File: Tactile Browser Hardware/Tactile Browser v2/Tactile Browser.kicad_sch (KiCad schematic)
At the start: 135 parts, among them SW1 SW_Push, SW10 SW_Push, SW11 SW_Push, SW12 SW_Push, SW13 SW_Push, SW14 SW_Push, SW15 SW_Push, SW16 SW_Push, SW17 SW_Push, SW18 SW_Push, SW2 SW_Push, SW3 SW_Push, SW4 SW_Push, SW5 SW_Push, SW6 SW_Push, SW7 SW_Push, SW8 SW_Push, SW9 SW_Push

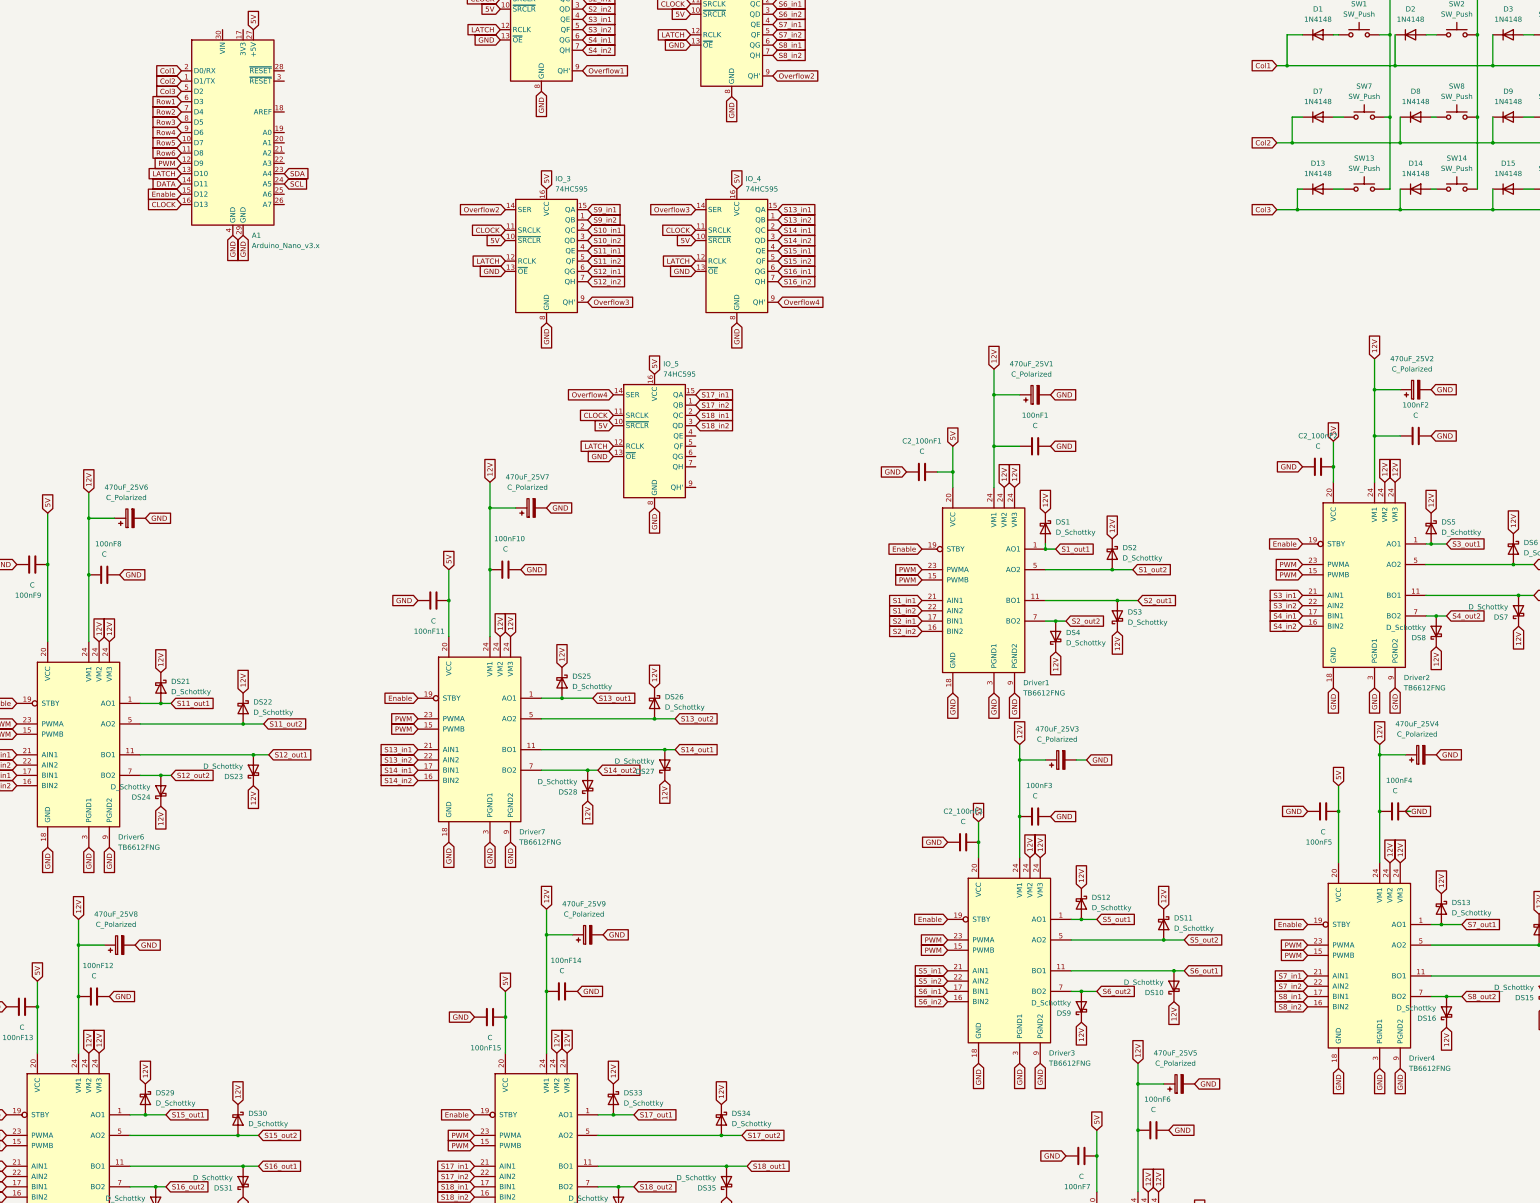
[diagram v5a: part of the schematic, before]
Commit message: updated capacitors
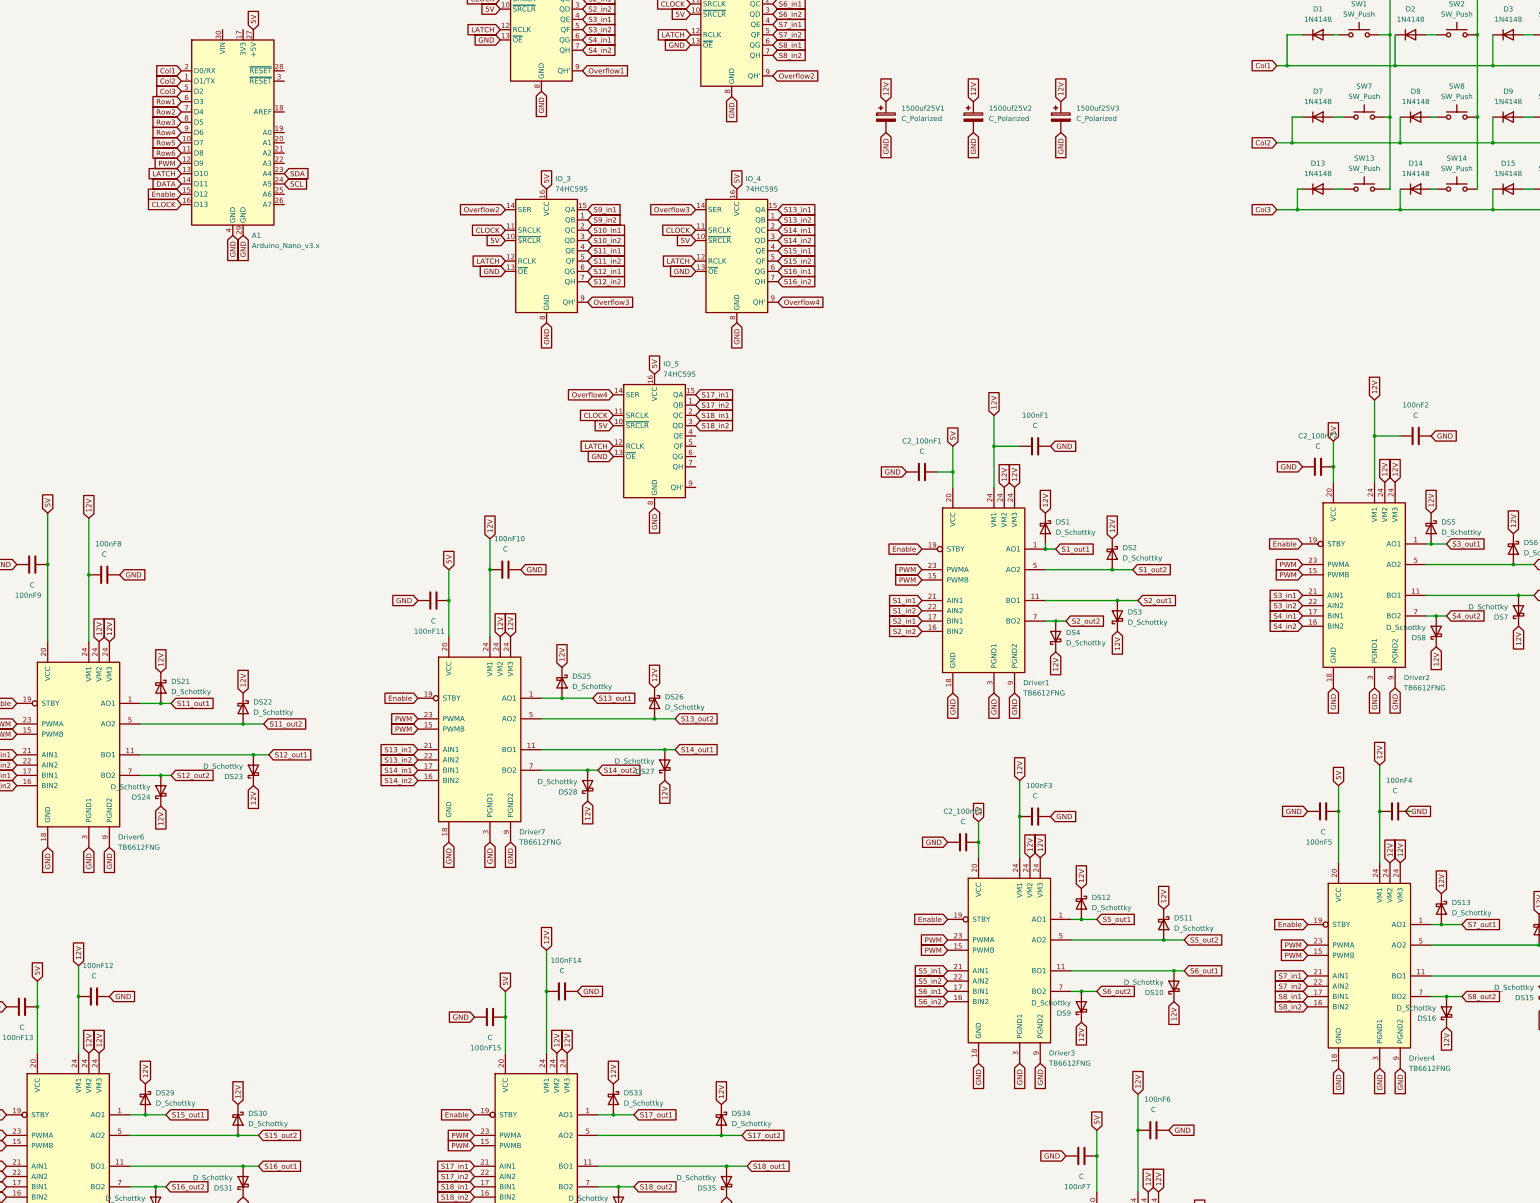
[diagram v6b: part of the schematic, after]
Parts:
- removed 470uF_25V1, 470uF_25V2, 470uF_25V3, 470uF_25V4, 470uF_25V5, 470uF_25V6, 470uF_25V7, 470uF_25V8, 470uF_25V9: C_Polarized, Capacitor_SMD:CP_Elec_8x10, symbol Device:C_Polarized
- added 1500uf25V1, 1500uf25V2, 1500uf25V3: C_Polarized, Capacitor_SMD:CP_Elec_8x10, symbol Device:C_Polarized
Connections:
- net 12V: now also 1500uf25V1.1, 1500uf25V2.1, 1500uf25V3.1
- net GND: now also 1500uf25V1.2, 1500uf25V2.2, 1500uf25V3.2

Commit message: changed to vertical screw terminals
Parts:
- removed 1500uf25V2, 1500uf25V3: C_Polarized, Capacitor_SMD:CP_Elec_8x10, symbol Device:C_Polarized
- added 1000uf25V2, 1000uf25V3, 1000uf25V4: C_Polarized, Capacitor_SMD:CP_Elec_10x12.5, symbol Device:C_Polarized
- 100uf25V1: renamed from 1500uf25V1; footprint Capacitor_SMD:CP_Elec_8x10 -> Capacitor_SMD:CP_Elec_10x12.5
- Sol1: renamed from Solenoid1; footprint TerminalBlock_Phoenix:TerminalBlock_Phoenix_MKDS-1,5-2-5.08_1x02_P5.08mm_Horizontal -> TerminalBlock_Phoenix:ScrewTerminal_Vertical_1935310
- Sol10: renamed from Solenoid10; footprint TerminalBlock_Phoenix:TerminalBlock_Phoenix_MKDS-1,5-2-5.08_1x02_P5.08mm_Horizontal -> TerminalBlock_Phoenix:ScrewTerminal_Vertical_1935310
- Sol11: renamed from Solenoid11; footprint TerminalBlock_Phoenix:TerminalBlock_Phoenix_MKDS-1,5-2-5.08_1x02_P5.08mm_Horizontal -> TerminalBlock_Phoenix:ScrewTerminal_Vertical_1935310
- Sol12: renamed from Solenoid12; footprint TerminalBlock_Phoenix:TerminalBlock_Phoenix_MKDS-1,5-2-5.08_1x02_P5.08mm_Horizontal -> TerminalBlock_Phoenix:ScrewTerminal_Vertical_1935310
- Sol13: renamed from Solenoid13; footprint TerminalBlock_Phoenix:TerminalBlock_Phoenix_MKDS-1,5-2-5.08_1x02_P5.08mm_Horizontal -> TerminalBlock_Phoenix:ScrewTerminal_Vertical_1935310
- Sol14: renamed from Solenoid14; footprint TerminalBlock_Phoenix:TerminalBlock_Phoenix_MKDS-1,5-2-5.08_1x02_P5.08mm_Horizontal -> TerminalBlock_Phoenix:ScrewTerminal_Vertical_1935310
- Sol15: renamed from Solenoid15; footprint TerminalBlock_Phoenix:TerminalBlock_Phoenix_MKDS-1,5-2-5.08_1x02_P5.08mm_Horizontal -> TerminalBlock_Phoenix:ScrewTerminal_Vertical_1935310
- Sol16: renamed from Solenoid16; footprint TerminalBlock_Phoenix:TerminalBlock_Phoenix_MKDS-1,5-2-5.08_1x02_P5.08mm_Horizontal -> TerminalBlock_Phoenix:ScrewTerminal_Vertical_1935310
- Sol17: renamed from Solenoid17; footprint TerminalBlock_Phoenix:TerminalBlock_Phoenix_MKDS-1,5-2-5.08_1x02_P5.08mm_Horizontal -> TerminalBlock_Phoenix:ScrewTerminal_Vertical_1935310
- Sol18: renamed from Solenoid18; footprint TerminalBlock_Phoenix:TerminalBlock_Phoenix_MKDS-1,5-2-5.08_1x02_P5.08mm_Horizontal -> TerminalBlock_Phoenix:ScrewTerminal_Vertical_1935310
- Sol2: renamed from Solenoid2; footprint TerminalBlock_Phoenix:TerminalBlock_Phoenix_MKDS-1,5-2-5.08_1x02_P5.08mm_Horizontal -> TerminalBlock_Phoenix:ScrewTerminal_Vertical_1935310
- Sol3: renamed from Solenoid3; footprint TerminalBlock_Phoenix:TerminalBlock_Phoenix_MKDS-1,5-2-5.08_1x02_P5.08mm_Horizontal -> TerminalBlock_Phoenix:ScrewTerminal_Vertical_1935310
- Sol4: renamed from Solenoid4; footprint TerminalBlock_Phoenix:TerminalBlock_Phoenix_MKDS-1,5-2-5.08_1x02_P5.08mm_Horizontal -> TerminalBlock_Phoenix:ScrewTerminal_Vertical_1935310
- Sol5: renamed from Solenoid5; footprint TerminalBlock_Phoenix:TerminalBlock_Phoenix_MKDS-1,5-2-5.08_1x02_P5.08mm_Horizontal -> TerminalBlock_Phoenix:ScrewTerminal_Vertical_1935310
- Sol6: renamed from Solenoid6; footprint TerminalBlock_Phoenix:TerminalBlock_Phoenix_MKDS-1,5-2-5.08_1x02_P5.08mm_Horizontal -> TerminalBlock_Phoenix:ScrewTerminal_Vertical_1935310
- Sol7: renamed from Solenoid7; footprint TerminalBlock_Phoenix:TerminalBlock_Phoenix_MKDS-1,5-2-5.08_1x02_P5.08mm_Horizontal -> TerminalBlock_Phoenix:ScrewTerminal_Vertical_1935310
- Sol8: renamed from Solenoid8; footprint TerminalBlock_Phoenix:TerminalBlock_Phoenix_MKDS-1,5-2-5.08_1x02_P5.08mm_Horizontal -> TerminalBlock_Phoenix:ScrewTerminal_Vertical_1935310
- Sol9: renamed from Solenoid9; footprint TerminalBlock_Phoenix:TerminalBlock_Phoenix_MKDS-1,5-2-5.08_1x02_P5.08mm_Horizontal -> TerminalBlock_Phoenix:ScrewTerminal_Vertical_1935310
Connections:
- net 12V: now also 1000uf25V2.1, 1000uf25V3.1, 1000uf25V4.1
- net GND: now also 1000uf25V2.2, 1000uf25V3.2, 1000uf25V4.2
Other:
- moved on the sheet: Sol15, Sol16

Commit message: solenoid wiring!!
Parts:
- 12V_supply1: footprint TerminalBlock_Altech:Altech_AK100_1x02_P5.00mm -> TerminalBlock_Phoenix:ScrewTerminal_Vertical_1935310
- 5V_logic_rail1, I2C_bus1: footprint TerminalBlock:TerminalBlock_Xinya_XY308-2.54-2P_1x02_P2.54mm_Horizontal -> Connector_JST:JST_PH_B2B-PH-SM4-TB_1x02-1MP_P2.00mm_Vertical
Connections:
- net Enable renamed STBY
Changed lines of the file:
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@@
 		)
 	)
-	(global_label "Enable"
+	(global_label "STBY"
 		(shape input)
 		(at 422.91 172.72 180)
@@
 		)
 		(property "Intersheetrefs" "${INTERSHEET_REFS}"
-			(at 413.575 172.72 0)
+			(at 415.3891 172.72 0)
 			(effects
 				(font
@@
 		)
 	)
-	(global_label "Enable"
+	(global_label "STBY"
 		(shape input)
 		(at 218.44 313.69 180)
@@
 		)
 		(property "Intersheetrefs" "${INTERSHEET_REFS}"
-			(at 209.105 313.69 0)
+			(at 210.9191 313.69 0)
 			(effects
 				(font
@@
 		)
 	)
-	(global_label "Enable"
+	(global_label "STBY"
 		(shape input)
 		(at 335.28 265.43 180)
@@
 		)
 		(property "Intersheetrefs" "${INTERSHEET_REFS}"
-			(at 325.945 265.43 0)
+			(at 327.7591 265.43 0)
 			(effects
 				(font
@@
 		)
 	)
-	(global_label "Enable"
+	(global_label "STBY"
 		(shape input)
 		(at 146.05 86.36 180)
@@
 		)
 		(property "Intersheetrefs" "${INTERSHEET_REFS}"
-			(at 136.715 86.36 0)
+			(at 138.5291 86.36 0)
 			(effects
 				(font
@@
 		)
 	)
-	(global_label "Enable"
+	(global_label "STBY"
 		(shape input)
 		(at 204.47 210.82 180)
@@
 		)
 		(property "Intersheetrefs" "${INTERSHEET_REFS}"
-			(at 195.135 210.82 0)
+			(at 196.9491 210.82 0)
 			(effects
 				(font
@@
 		)
 	)
-	(global_label "Enable"
+	(global_label "STBY"
 		(shape input)
 		(at 424.18 266.7 180)
@@
 		)
 		(property "Intersheetrefs" "${INTERSHEET_REFS}"
-			(at 414.845 266.7 0)
+			(at 416.6591 266.7 0)
 			(effects
 				(font
@@
 		)
 	)
-	(global_label "Enable"
+	(global_label "STBY"
 		(shape input)
 		(at 364.49 347.98 180)
@@
 		)
 		(property "Intersheetrefs" "${INTERSHEET_REFS}"
-			(at 355.155 347.98 0)
+			(at 356.9691 347.98 0)
 			(effects
 				(font
@@
 		)
 	)
-	(global_label "Enable"
+	(global_label "STBY"
 		(shape input)
 		(at 105.41 212.09 180)
@@
 		)
 		(property "Intersheetrefs" "${INTERSHEET_REFS}"
-			(at 96.075 212.09 0)
+			(at 97.8891 212.09 0)
 			(effects
 				(font
@@
 		)
 	)
-	(global_label "Enable"
+	(global_label "STBY"
 		(shape input)
 		(at 102.87 313.69 180)
@@
 		)
 		(property "Intersheetrefs" "${INTERSHEET_REFS}"
-			(at 93.535 313.69 0)
+			(at 95.3491 313.69 0)
 			(effects
 				(font
@@
 		)
 	)
-	(global_label "Enable"
+	(global_label "STBY"
 		(shape input)
 		(at 328.93 173.99 180)
@@
 		)
 		(property "Intersheetrefs" "${INTERSHEET_REFS}"
-			(at 319.595 173.99 0)
+			(at 321.4091 173.99 0)
 			(effects
 				(font
@@
 			)
 		)
-		(property "Footprint" "TerminalBlock_Altech:Altech_AK100_1x02_P5.00mm"
+		(property "Footprint" "TerminalBlock_Phoenix:ScrewTerminal_Vertical_1935310"
 			(at 24.13 24.13 0)
 			(effects
@@
 			)
 		)
-		(property "Footprint" "TerminalBlock:TerminalBlock_Xinya_XY308-2.54-2P_1x02_P2.54mm_Horizontal"
+		(property "Footprint" "Connector_JST:JST_PH_B2B-PH-SM4-TB_1x02-1MP_P2.00mm_Vertical"
 			(at 44.45 25.4 0)
 			(effects
@@
 			)
 		)
-		(property "Footprint" "TerminalBlock:TerminalBlock_Xinya_XY308-2.54-2P_1x02_P2.54mm_Horizontal"
+		(property "Footprint" "Connector_JST:JST_PH_B2B-PH-SM4-TB_1x02-1MP_P2.00mm_Vertical"
 			(at 66.04 26.67 0)
 			(effects
